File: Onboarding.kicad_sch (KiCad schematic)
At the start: 0 parts

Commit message: Created example branch, started annotations
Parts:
- added C10, C11, C8, C9: 10u, Capacitor_SMD:C_1206_3216Metric_Pad1.33x1.80mm_HandSolder, symbol Device:C
- added C2: 100p, Capacitor_SMD:C_0603_1608Metric_Pad1.08x0.95mm_HandSolder, symbol Device:C_Small
- added C4: 1u, Capacitor_SMD:C_0603_1608Metric_Pad1.08x0.95mm_HandSolder, symbol Device:C
- added C6: 0.01u, Capacitor_SMD:C_0603_1608Metric_Pad1.08x0.95mm_HandSolder, symbol Device:C_Small
- added D1: BAT54, Package_TO_SOT_SMD:SOT-23_Handsoldering, symbol Device:D_Schottky
- added J1: Conn_01x02, Connector_AMASS:AMASS_XT30U-F_1x02_P5.0mm_Vertical, symbol Connector_Generic:Conn_01x02
- added J2: Conn_01x02, Connector_AMASS:AMASS_XT30U-M_1x02_P5.0mm_Vertical, symbol Connector_Generic:Conn_01x02
- added L1: 220u, ! Robomaster Passives:ASPIAIGS6055221MT, symbol Device:L_Iron_Small
- added R1: 180, Resistor_SMD:R_0805_2012Metric_Pad1.20x1.40mm_HandSolder, symbol Device:R_Small
- added R3: 1, Resistor_SMD:R_0603_1608Metric_Pad0.98x0.95mm_HandSolder, symbol Device:R_Small
- added R5, R9: 22k, Resistor_SMD:R_0603_1608Metric_Pad0.98x0.95mm_HandSolder, symbol Device:R_Small
- added R8: 1k, Resistor_SMD:R_0603_1608Metric_Pad0.98x0.95mm_HandSolder, symbol Device:R_Small
- added TP2: V_{C}, TestPoint:TestPoint_Bridge_Pitch2.0mm_Drill0.7mm, symbol Connector:TestPoint
- added TP3: V_{E}, TestPoint:TestPoint_Pad_1.0x1.0mm, symbol Connector:TestPoint
- added U2: MC34063A, Package_SO:SOIC-8_3.9x4.9mm_P1.27mm, symbol ! Robomaster ICs:MC34063A
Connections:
- new net: D1.1 (A), L1.1, TP3.1, U2.1 (SC)
- new net: L1.2, R1.1, R3.2, TP2.1, U2.7 (I_{PK})
- new net: C6.1, R5.1, R8.1, R9.1, U2.5 (COMP-)
- new net: C2.1, U2.3 (CT)
- new net: R1.2, U2.8 (DC)
- new net +24V: C4.1, J1.1 (Pin_1), R3.1, U2.6 (VCC)
- new net GND: C10.2, C11.2, C2.2, C4.2, C8.2, C9.2, J1.2 (Pin_2), J2.2 (Pin_2), R8.2, R9.2, U2.2 (SE), U2.4 (GND)
- new net VCC: C10.1, C11.1, C6.2, C8.1, C9.1, D1.3 (K), J2.1 (Pin_1), R5.2
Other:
- note added: "*Power inputs should always be XT-30 Female!"
- note added: "*Power outputs should always be XT-30 Male!"
- note added: "Current Sense"
- note added: "Input Power"
- note added: "Input filtering"
- note added: "No filter (reduced ringing)"
- note added: "Output Power"
- note added: "VOUT = 1.25 * (1 + ^{Rtop}/_{Rbot}) = 30.0 V"
- note added: "~7.7 mV ripple (with filter)"

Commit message: finishing example schematic
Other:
- note added: "Charge collection"
- note added: "Switching"
- note added: "Voltage Divider _{(Comparator feedback)}"
- moved on the sheet: C4
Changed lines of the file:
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@@
 	)
 	(rectangle
-		(start 62.23 38.1)
-		(end 82.55 74.93)
+		(start 68.58 38.1)
+		(end 88.9 72.39)
 		(stroke
 			(width 0)
@@
 		)
 	)
+	(rectangle
+		(start 149.86 55.88)
+		(end 201.93 86.36)
+		(stroke
+			(width 0)
+			(type dot)
+		)
+		(fill
+			(type none)
+		)
+	)
+	(rectangle
+		(start 110.49 72.39)
+		(end 142.24 107.95)
+		(stroke
+			(width 0)
+			(type dot)
+		)
+		(fill
+			(type none)
+		)
+	)
+	(text "Voltage Divider\n_{(Comparator feedback)}"
+		(exclude_from_sim no)
+		(at 110.744 74.93 0)
+		(effects
+			(font
+				(size 1.27 1.27)
+			)
+			(justify left)
+		)
+	)
 	(text "Input filtering"
 		(exclude_from_sim no)
-		(at 62.992 39.878 0)
+		(at 69.342 39.878 0)
+		(effects
+			(font
+				(size 1.27 1.27)
+			)
+			(justify left)
+		)
+	)
+	(text "Switching"
+		(exclude_from_sim no)
+		(at 113.538 41.148 0)
+		(effects
+			(font
+				(size 1.27 1.27)
+			)
+			(justify left)
+		)
+	)
+	(text "Charge collection"
+		(exclude_from_sim no)
+		(at 150.622 57.912 0)
 		(effects
 			(font
@@
 	(text "No filter\n(reduced ringing)"
 		(exclude_from_sim no)
-		(at 177.292 44.196 0)
+		(at 211.582 58.42 0)
 		(effects
 			(font
@@
 	(text "Current Sense"
 		(exclude_from_sim no)
-		(at 85.852 37.592 0)
+		(at 90.932 37.338 0)
 		(effects
 			(font
@@
 	)
 	(junction
-		(at 73.66 52.07)
+		(at 80.01 52.07)
 		(diameter 0)
 		(color 0 0 0 0)
@@
 	(wire
 		(pts
-			(xy 73.66 49.53) (xy 73.66 52.07)
+			(xy 80.01 49.53) (xy 80.01 52.07)
 		)
 		(stroke
@@
 		)
 	)
+	(polyline
+		(pts
+			(xy 113.03 44.45) (xy 125.73 44.45)
+		)
+		(stroke
+			(width 0)
+			(type dot)
+		)
+	)
 	(wire
 		(pts
@@
 		)
 	)
+	(polyline
+		(pts
+			(xy 137.16 49.53) (xy 125.73 49.53)
+		)
+		(stroke
+			(width 0)
+			(type dot)
+		)
+	)
 	(wire
 		(pts
@@
 	(wire
 		(pts
-			(xy 73.66 52.07) (xy 95.25 52.07)
+			(xy 80.01 52.07) (xy 95.25 52.07)
 		)
 		(stroke
@@
 		)
 	)
+	(polyline
+		(pts
+			(xy 125.73 49.53) (xy 125.73 44.45)
+		)
+		(stroke
+			(width 0)
+			(type dot)
+		)
+	)
+	(polyline
+		(pts
+			(xy 113.03 44.45) (xy 113.03 39.37)
+		)
+		(stroke
+			(width 0)
+			(type dot)
+		)
+	)
 	(wire
 		(pts
@@
 	(wire
 		(pts
-			(xy 73.66 62.23) (xy 73.66 64.77)
+			(xy 80.01 62.23) (xy 80.01 64.77)
 		)
 		(stroke
@@
 	(polyline
 		(pts
-			(xy 85.09 35.56) (xy 85.09 53.34)
+			(xy 90.17 35.56) (xy 90.17 53.34)
 		)
 		(stroke
@@
 	(wire
 		(pts
-			(xy 73.66 52.07) (xy 73.66 54.61)
+			(xy 80.01 52.07) (xy 80.01 54.61)
 		)
 		(stroke
@@
 		)
 	)
+	(polyline
+		(pts
+			(xy 137.16 39.37) (xy 137.16 49.53)
+		)
+		(stroke
+			(width 0)
+			(type dot)
+		)
+	)
 	(wire
 		(pts
@@
 	(polyline
 		(pts
-			(xy 85.09 35.56) (xy 109.22 35.56)
+			(xy 90.17 35.56) (xy 109.22 35.56)
 		)
 		(stroke
@@
 	(polyline
 		(pts
-			(xy 85.09 53.34) (xy 124.46 53.34)
+			(xy 113.03 39.37) (xy 137.16 39.37)
+		)
+		(stroke
+			(width 0)
+			(type dot)
+		)
+	)
+	(polyline
+		(pts
+			(xy 90.17 53.34) (xy 124.46 53.34)
 		)
 		(stroke
@@
 	(symbol
 		(lib_id "power:GND")
-		(at 73.66 64.77 0)
+		(at 80.01 64.77 0)
 		(unit 1)
 		(exclude_from_sim no)
@@
 		(fields_autoplaced yes)
 		(property "Reference" "#PWR0111"
-			(at 73.66 71.12 0)
+			(at 80.01 71.12 0)
 			(effects
 				(font
@@
 		)
 		(property "Value" "GND"
-			(at 73.66 69.85 0)
+			(at 80.01 69.85 0)
 			(effects
 				(font
@@
 		)
 		(property "Footprint" ""
-			(at 73.66 64.77 0)
+			(at 80.01 64.77 0)
 			(effects
 				(font
@@
 		)
 		(property "Datasheet" ""
-			(at 73.66 64.77 0)
+			(at 80.01 64.77 0)
 			(effects
 				(font
@@
 		)
 		(property "Description" "Power symbol creates a global label with name \"GND\" , ground"
-			(at 73.66 64.77 0)
+			(at 80.01 64.77 0)
 			(effects
 				(font
@@
 	(symbol
 		(lib_id "power:+24V")
-		(at 73.66 49.53 0)
+		(at 80.01 49.53 0)
 		(unit 1)
 		(exclude_from_sim no)
@@
 		(fields_autoplaced yes)
 		(property "Reference" "#PWR06"
-			(at 73.66 53.34 0)
+			(at 80.01 53.34 0)
 			(effects
 				(font
@@
 		)
 		(property "Value" "+24V"
-			(at 73.66 44.45 0)
+			(at 80.01 44.45 0)
 			(effects
 				(font
@@
 		)
 		(property "Footprint" ""
-			(at 73.66 49.53 0)
+			(at 80.01 49.53 0)
 			(effects
 				(font
@@
 		)
 		(property "Datasheet" ""
-			(at 73.66 49.53 0)
+			(at 80.01 49.53 0)
 			(effects
 				(font
@@
 		)
 		(property "Description" "Power symbol creates a global label with name \"+24V\""
-			(at 73.66 49.53 0)
+			(at 80.01 49.53 0)
 			(effects
 				(font
@@
 	(symbol
 		(lib_id "Device:C")
-		(at 73.66 58.42 0)
+		(at 80.01 58.42 0)
 		(mirror y)
 		(unit 1)
@@
 		(dnp no)
 		(property "Reference" "C4"
-			(at 69.85 57.1499 0)
+			(at 76.2 57.1499 0)
 			(effects
 				(font
@@
 		)
 		(property "Value" "1u"
-			(at 69.85 59.6899 0)
+			(at 76.2 59.6899 0)
 			(effects
 				(font
@@
 		)
 		(property "Footprint" "Capacitor_SMD:C_0603_1608Metric_Pad1.08x0.95mm_HandSolder"
-			(at 72.6948 62.23 0)
+			(at 79.0448 62.23 0)
 			(effects
 				(font
@@
 		)
 		(property "Datasheet" "https://www.mouser.com/datasheet/2/447/KEM_C1006_X5R_SMD-3316465.pdf"
-			(at 73.66 58.42 0)
+			(at 80.01 58.42 0)
 			(effects
 				(font
@@
 		)
 		(property "Description" "Unpolarized capacitor"
-			(at 73.66 58.42 0)
+			(at 80.01 58.42 0)
 			(effects
 				(font
@@
 		)
 		(property "Mouser Part Number" "963-UMK107BJ105KA-T"
-			(at 73.66 58.42 0)
+			(at 80.01 58.42 0)
 			(effects
 				(font
@@
 		)
 		(property "Height" ""
-			(at 73.66 58.42 0)
+			(at 80.01 58.42 0)
 			(effects
 				(font
@@
 		)
 		(property "Manufacturer_Name" ""
-			(at 73.66 58.42 0)
+			(at 80.01 58.42 0)
 			(effects
 				(font
@@
 		)
 		(property "Manufacturer_Part_Number" ""
-			(at 73.66 58.42 0)
+			(at 80.01 58.42 0)
 			(effects
 				(font
@@
 		)
 		(property "Mouser Price/Stock" ""
-			(at 73.66 58.42 0)
+			(at 80.01 58.42 0)
 			(effects
 				(font
@@
 		)
 		(property "Voltage Rating" "50V"
-			(at 69.85 62.484 0)
+			(at 76.2 62.484 0)
 			(effects
 				(font

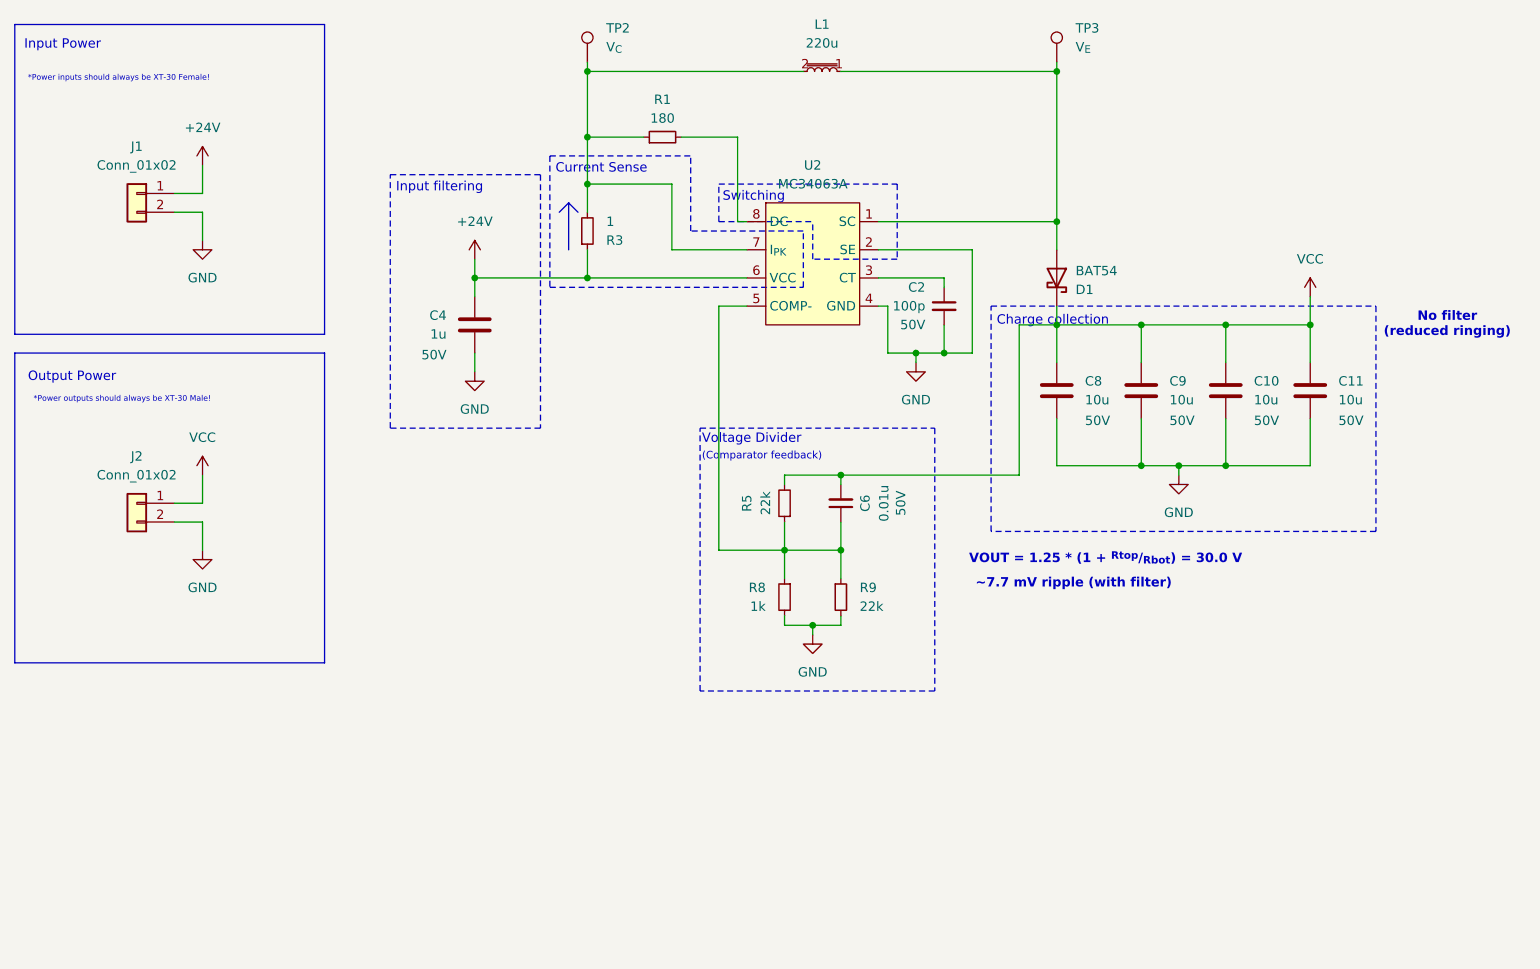
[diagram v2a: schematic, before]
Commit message: Finished example schematic and component layout
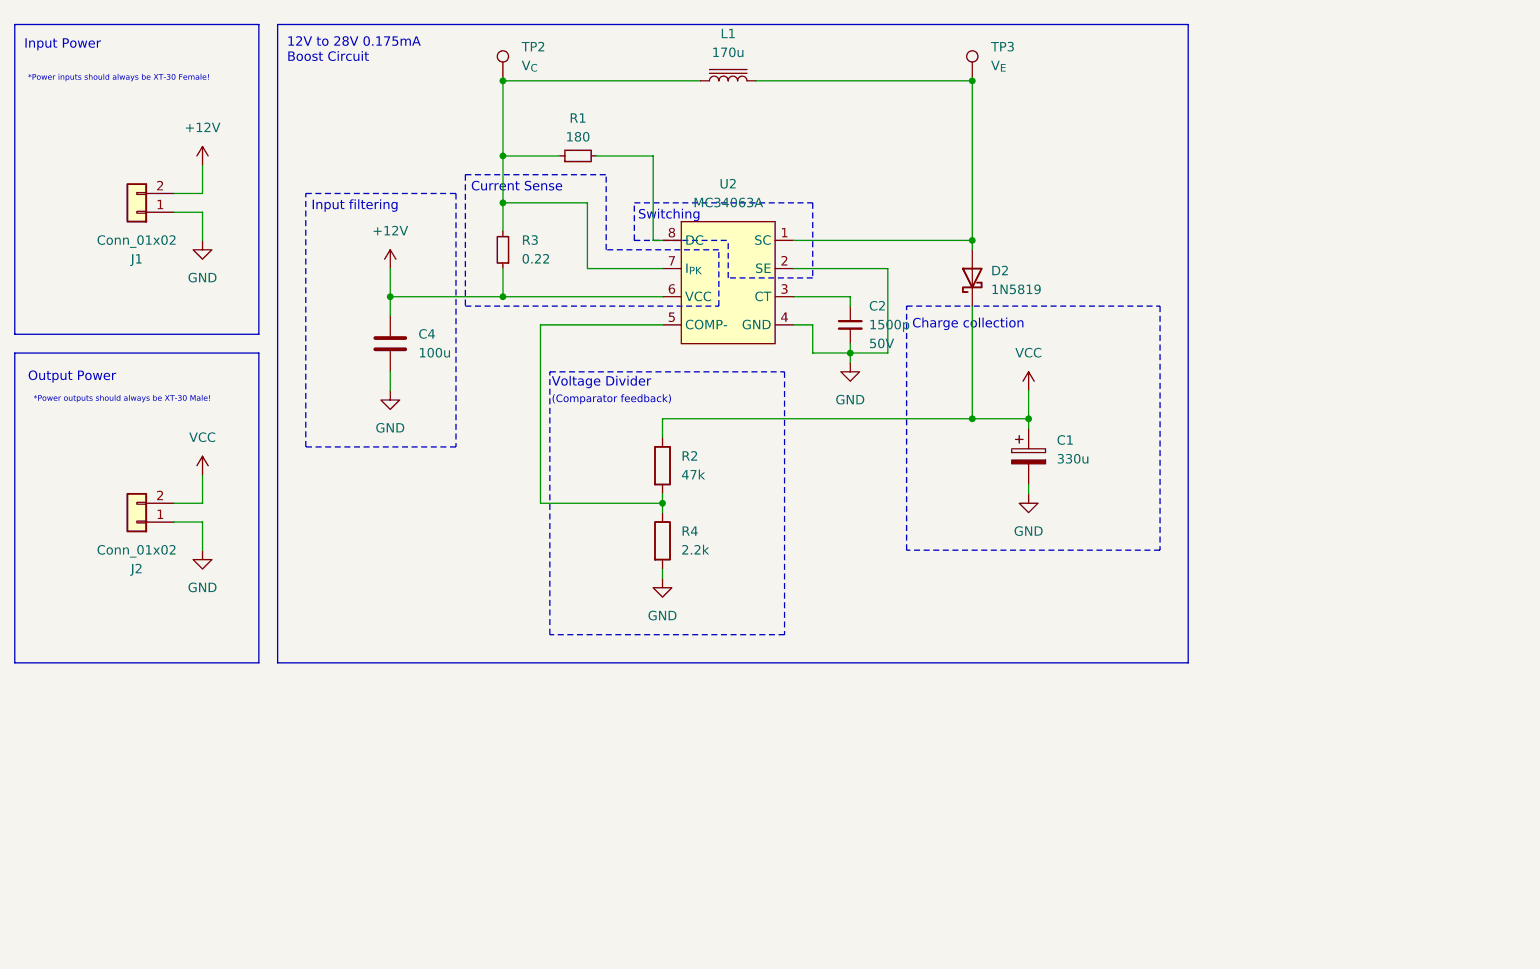
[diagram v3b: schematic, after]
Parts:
- removed C10, C11, C8, C9: 10u, Capacitor_SMD:C_1206_3216Metric_Pad1.33x1.80mm_HandSolder, symbol Device:C
- removed C6: 0.01u, Capacitor_SMD:C_0603_1608Metric_Pad1.08x0.95mm_HandSolder, symbol Device:C_Small
- removed D1: BAT54, Package_TO_SOT_SMD:SOT-23_Handsoldering, symbol Device:D_Schottky
- removed L1: 220u, ! Robomaster Passives:ASPIAIGS6055221MT, symbol Device:L_Iron_Small
- removed R5, R9: 22k, Resistor_SMD:R_0603_1608Metric_Pad0.98x0.95mm_HandSolder, symbol Device:R_Small
- removed R8: 1k, Resistor_SMD:R_0603_1608Metric_Pad0.98x0.95mm_HandSolder, symbol Device:R_Small
- added C1: 330u, Capacitor_THT:CP_Radial_D8.0mm_P5.00mm, symbol Device:C_Polarized
- added D2: 1N5819, Diode_SMD:D_SOD-123F, symbol Diode:1N5819
- added L1: 170u, Inductor_SMD:L_Sunlord_SWPA8040S, symbol Device:L_Iron
- added R2: 47k, Resistor_SMD:R_0603_1608Metric_Pad0.98x0.95mm_HandSolder, symbol Device:R
- added R4: 2.2k, Resistor_SMD:R_0603_1608Metric_Pad0.98x0.95mm_HandSolder, symbol Device:R
- C2: value 100p -> 1500p
- C4: value 1u -> 100u; footprint Capacitor_SMD:C_0603_1608Metric_Pad1.08x0.95mm_HandSolder -> Capacitor_SMD:C_0805_2012Metric; Mouser Part Number 963-UMK107BJ105KA-T -> (none); Voltage Rating 50V -> (none)
- R3: value 1 -> 0.22
- TP3: footprint TestPoint:TestPoint_Pad_1.0x1.0mm -> TestPoint:TestPoint_Bridge_Pitch2.0mm_Drill0.7mm
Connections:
- net GND: now also J1.1 (Pin_1), J2.1 (Pin_1), C1.2, R4.2; no longer J1.2 (Pin_2), J2.2 (Pin_2)
- net VCC: now also J2.2 (Pin_2), C1.1, D2.1 (K), R2.1; no longer J2.1 (Pin_1)
- net at TP3.1, U2.1 (SC): now also D2.2 (A), L1.2
- net at R1.1, R3.2, TP2.1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: now also L1.1
- net at U2.5 (COMP-): now also R2.2, R4.1
- net +24V renamed +12V
- net +12V: now also J1.2 (Pin_2); no longer J1.1 (Pin_1)
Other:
- note added: "12V to 28V 0.175mA Boost Circuit"
- note removed: "No filter (reduced ringing)"
- note removed: "VOUT = 1.25 * (1 + ^{Rtop}/_{Rbot}) = 30.0 V"
- note removed: "~7.7 mV ripple (with filter)"
- moved on the sheet: C2, J1, J2, R1, R3, TP2, TP3, U2

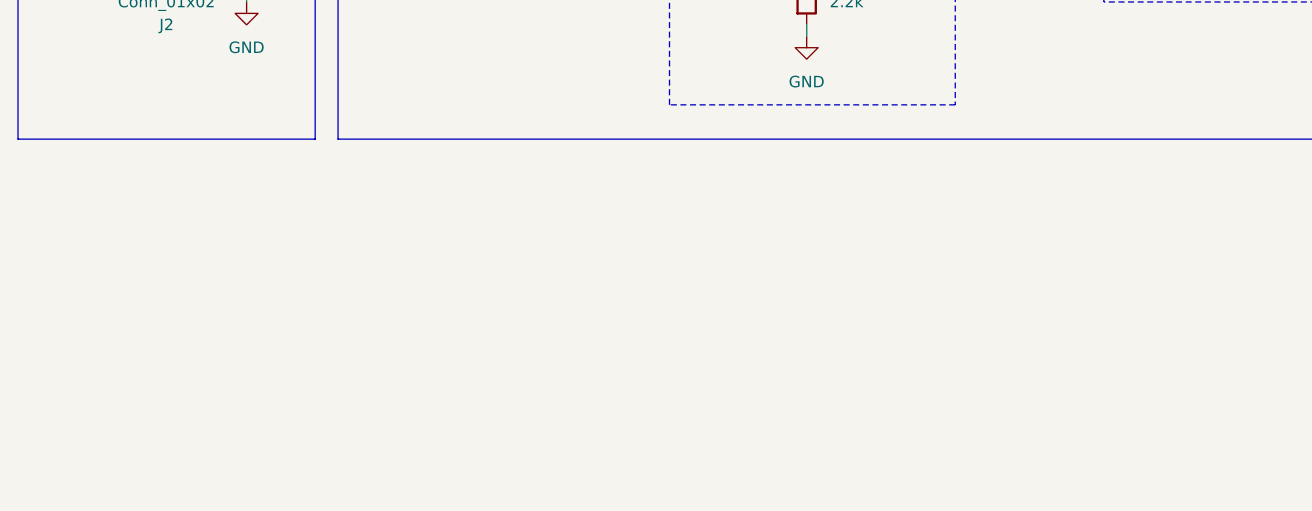
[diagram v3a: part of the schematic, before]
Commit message: Finished onboarding example layout
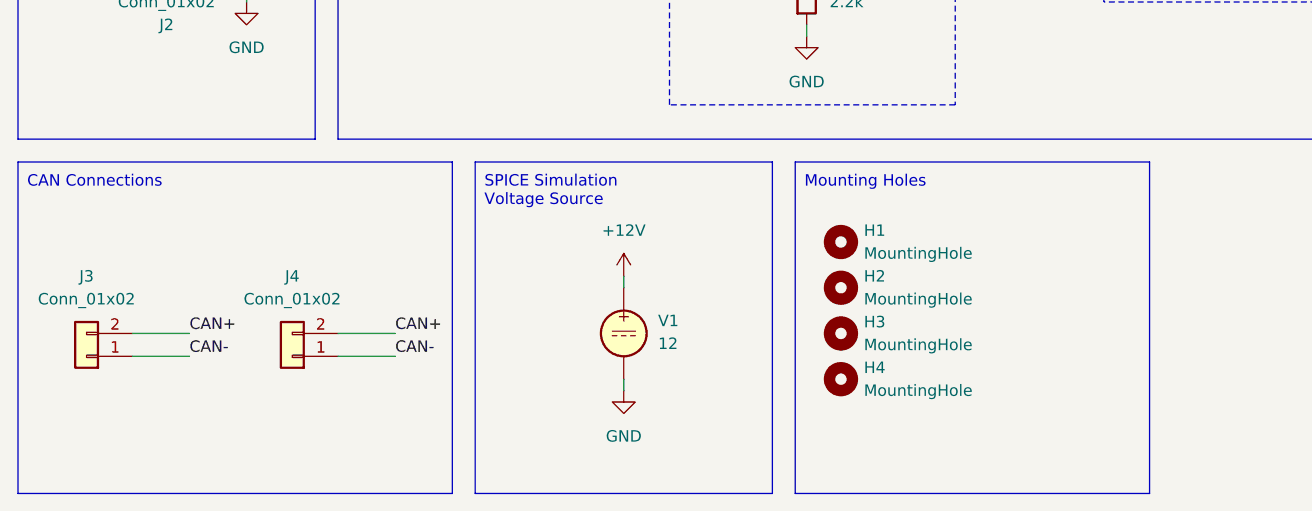
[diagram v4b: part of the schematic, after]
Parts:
- added H1, H2, H3, H4: MountingHole, MountingHole:MountingHole_2.2mm_M2, symbol Mechanical:MountingHole
- added J3, J4: Conn_01x02, Connector_JST:JST_GH_BM02B-GHS-TBT_1x02-1MP_P1.25mm_Vertical, symbol Connector_Generic:Conn_01x02
- added V1: 12, symbol Simulation_SPICE:VDC
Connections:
- net +12V: now also V1.1
- net GND: now also V1.2
- new net CAN+: J3.2 (Pin_2), J4.2 (Pin_2)
- new net CAN-: J3.1 (Pin_1), J4.1 (Pin_1)
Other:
- note added: "CAN Connections"
- note added: "Mounting Holes"
- note added: "SPICE Simulation Voltage Source"
